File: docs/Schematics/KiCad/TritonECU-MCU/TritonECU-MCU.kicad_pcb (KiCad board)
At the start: 6 copper layers, 44 x 44 mm, 38 parts, among them J1 Header A, J2 Header B, J3 Header C, J4 Header D, J5 STDC14 SWD+VCP, U1 STM32F767ZIT6, Y1 8MHz, Y2 32.768kHz

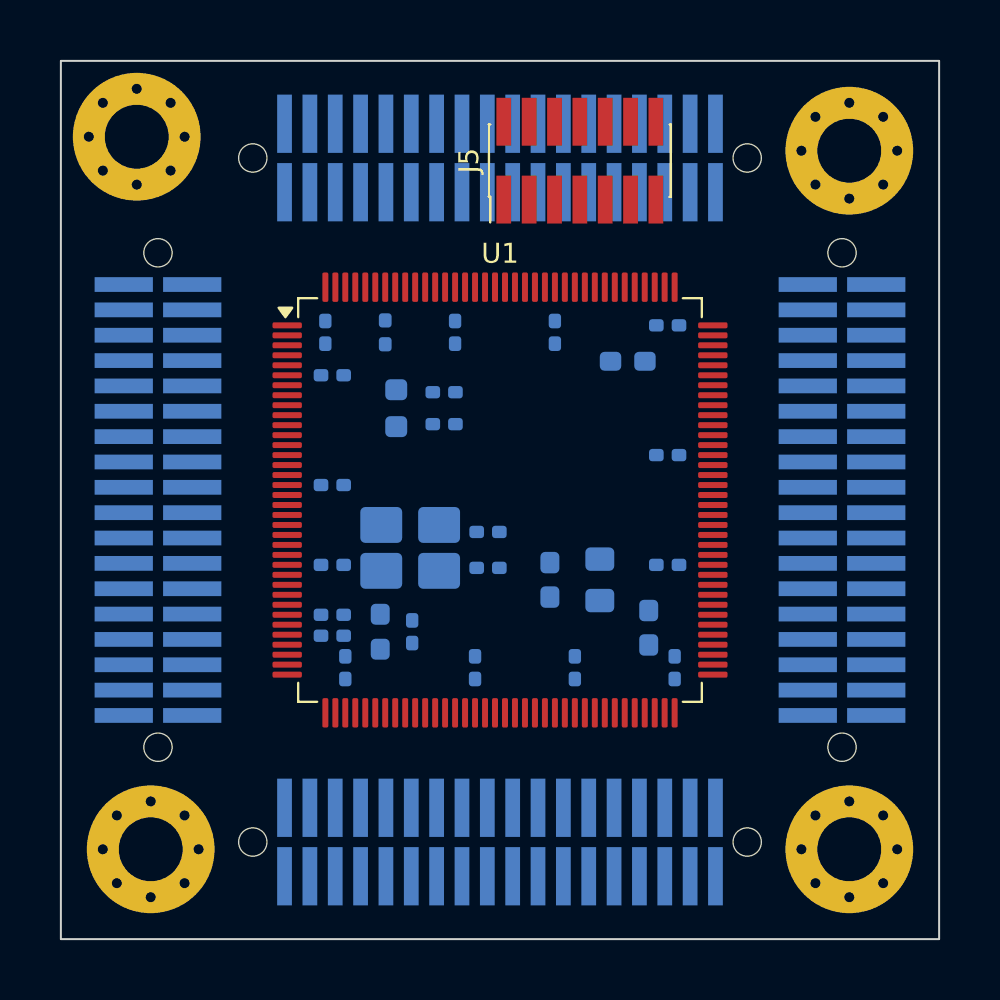
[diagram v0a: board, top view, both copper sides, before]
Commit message: MCU module: route 46 mm board on Samtec FTSH/FLE with Wurth/PEM standoffs
- Interconnect: FTSH-118-02-L-DV-A (module bottom) mating FLE-118-01-G-DV-K-TR
  (carrier top), 7.47 mm stack, replacing TFM-118-22 / SFM-118-02. FTSH pads
  trimmed 0.1 mm at the inner end for the 0.25 mm hole clearance to the -A
  alignment holes.
- Standoffs: Wurth 9774050982R 5 mm SMT spacer on the module, PEM
  SMTSO-M3-2ET 2 mm on the carrier, 0.5 mm M3 washer between (7.5 mm),
  M3 x 10 screw. Spacer footprint generated from the Wurth land pattern with
  a GND ring, plus Wurth's STEP model.
- Module grows 44 -> 46 mm for the spacer pads; H1 keying offset now inward.
- Board routed with Freerouting: DRC 0 violations, 0 unconnected, schematic
  parity clean. All parts included in the BOM; supplier BOM exports added.
- Generators: fix footprint-to-symbol links (netlist tstamps regex), copy all
  schematic fields, skip no-connect pins, footprint-only mode in gen_module.py,
  carrier floor plan refreshes a changed mate footprint in place.

Co-Authored-By: Claude Opus 5.5 <noreply@anthropic.com>
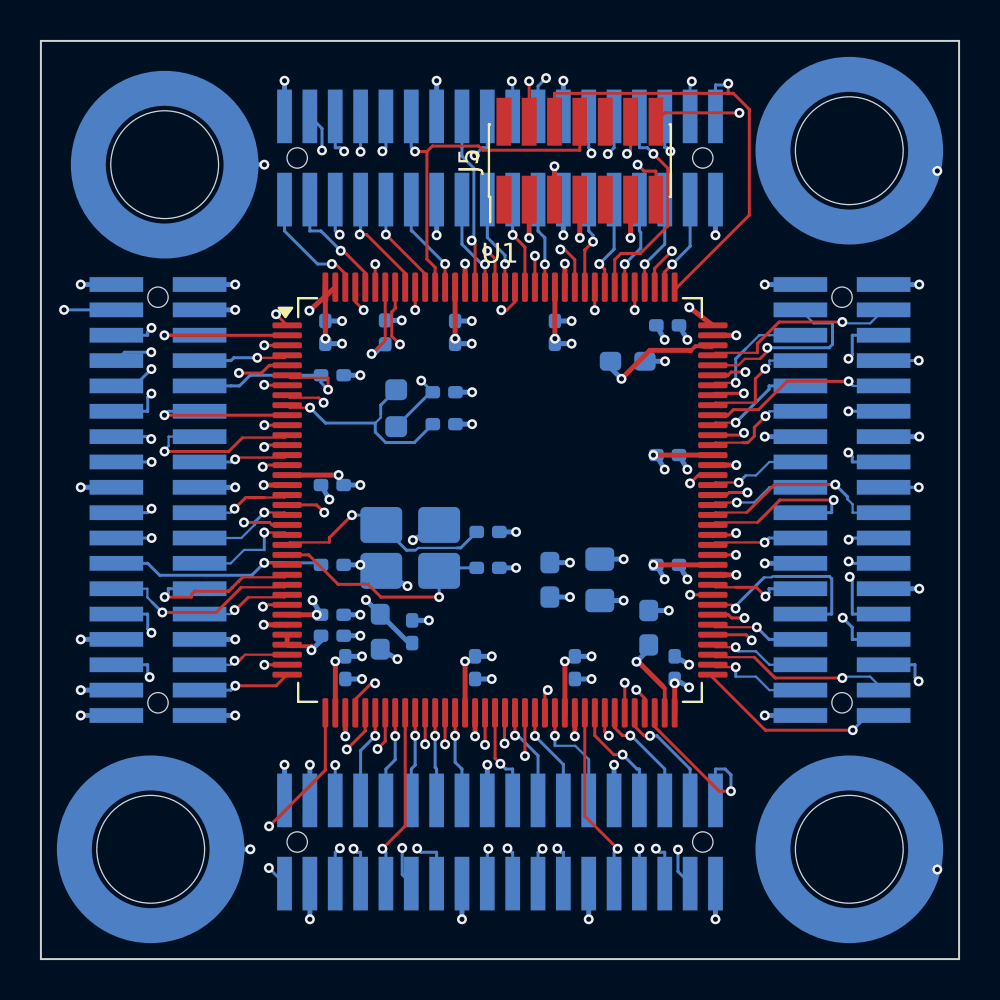
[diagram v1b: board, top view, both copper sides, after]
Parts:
- C21, C22: value 10p -> 27p
- C23, C24: value 10p -> 18p
- H1, H2, H3, H4: value M3 standoff -> Spacer 5mm; footprint MountingHole:MountingHole_3.2mm_M3_Pad_Via -> TritonECU-MCU:Wurth_WA-SMST_9774050982R; moved to B.Cu
- J1: value Header A -> ~; footprint TritonECU-MCU:Samtec_TFM-118-22-L-D-A -> TritonECU-MCU:Samtec_FTSH-118-02-L-DV-A
- J2: value Header B -> ~; footprint TritonECU-MCU:Samtec_TFM-118-22-L-D-A -> TritonECU-MCU:Samtec_FTSH-118-02-L-DV-A
- J3: value Header C -> ~; footprint TritonECU-MCU:Samtec_TFM-118-22-L-D-A -> TritonECU-MCU:Samtec_FTSH-118-02-L-DV-A
- J4: value Header D -> ~; footprint TritonECU-MCU:Samtec_TFM-118-22-L-D-A -> TritonECU-MCU:Samtec_FTSH-118-02-L-DV-A
- moved H1 1.98 mm to (83.2, 83.2)
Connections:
- J5 pad 1: unconnected-(J5-NC-Pad1) -> (no net)
- J5 pad 10: unconnected-(J5-JTDI/NC-Pad10) -> (no net)
- J5 pad 2: unconnected-(J5-NC-Pad2) -> (no net)
- J5 pad 9: unconnected-(J5-JRCLK/NC-Pad9) -> (no net)
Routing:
- net GND: track 0.00 -> 86.3 mm, vias 0 -> 63
- net +3.3V: track 0.00 -> 61.2 mm, vias 0 -> 41
- net /PD8: track 0.00 -> 45.7 mm, vias 0 -> 3
- net /NRST: track 0.00 -> 44.7 mm, vias 0 -> 2
- net /PD9: track 0.00 -> 33.8 mm, vias 0 -> 2
- net /PA13: track 0.00 -> 32.8 mm, vias 0 -> 2
- net /PA14: track 0.00 -> 24.8 mm, vias 0 -> 1
- net /PB3: track 0.00 -> 18.7 mm, vias 0 -> 1
- net /PE2: track 0.00 -> 15.5 mm, vias 0 -> 2
- net /PB7: track 0.00 -> 15.4 mm, vias 0 -> 2
- net /PG10: track 0.00 -> 15.3 mm, vias 0 -> 2
- net /PF7: track 0.00 -> 13.0 mm, vias 0 -> 2
- net /BOOT0: track 0.00 -> 13.0 mm, vias 0 -> 2
- net /PD12: track 0.00 -> 13.0 mm, vias 0 -> 2
- net /PG6: track 0.00 -> 13.0 mm, vias 0 -> 2
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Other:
- board size 44 x 44 mm -> 46 x 46 mm
- board text added: "Headers: Samtec FTSH-118-02-L-DV-A SMT on the bottom (vendor pad geometry)"
- board text removed: "Headers: Samtec TFM-118-22 SMT on the bottom (vendor pad geometry)"
